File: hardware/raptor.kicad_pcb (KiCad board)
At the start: 4 copper layers, 22.9 x 57.7 mm, 70 parts, among them IC1 RAPTORQFN56, IC2 FT232H, IC3 MCP1755, IC4 93C56, IC5 TMUX1574RSVR, J1 USB, J11 CONN_20, J12 CONN_20, J2 Conn_01x02_Male, J3 Conn_01x02_Male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

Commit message: raptor hardware rev c
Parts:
- added U4: SN74LV1T34DCKR, parts and footprints:SOT65P210X110-5N, B.Cu at (141.5, 126.2)
- added U5: SN74LV1T34DCKR, parts and footprints:SOT65P210X110-5N, B.Cu at (145.9, 126.1)
- X1: footprint SamacSys_Parts:CSTNE12M0GH5L000R0 -> parts and footprints:CSTNE12M0GH5L000R0
- X2: value CSTNE12M0GH5L000R0 -> CSTCR6M25G55B-R0; footprint SamacSys_Parts:CSTNE12M0GH5L000R0 -> parts and footprints:CSTCR6M25G55BR0
- moved R24 3.77 mm to (147.7, 129.0), turned to 180 degrees
- moved X2 0.25 mm to (153.9, 112.9)
- moved U3 0.09 mm to (147.7, 130.9), turned to 180 degrees
- renumbered U1 to U3
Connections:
- IC2 pad 26: Net-(IC2-Pad26) -> Net-(D6-Pad1)
- IC2 pad 27: Net-(IC2-Pad27) -> Net-(D5-Pad1)
- IC2 pad 32: Net-(D6-Pad1) -> Net-(IC2-Pad32)
- IC2 pad 33: Net-(D5-Pad1) -> Net-(IC2-Pad33)
- IC5 pad 1: /RAPTOR_CS -> /USB_CS
- IC5 pad 16: /USB_CS -> /RAPTOR_CS
- IC5 pad 3: /USB_SI -> /RAPTOR_D1
- IC5 pad 4: /RAPTOR_D1 -> /USB_SI
- J12 pad 17: /PWM0 -> /PWM0_LV
- J12 pad 18: /PWM1 -> /PWM1_LV
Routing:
- net /TXD_EN: track 52.5 -> 69.5 mm
- net /USB_SO_RXD: track 53.4 -> 69.9 mm, vias 3 -> 4
- net GND: track 246.9 -> 260.5 mm, vias 12 -> 14
- net VDD: track 252.7 -> 265.7 mm
- net /PWM1_LV: track 0.00 -> 10.6 mm
- net /P0: track 62.0 -> 64.9 mm
- net /PWM0_LV: track 0.00 -> 2.82 mm
- net Net-(D5-Pad1): track 4.48 -> 7.25 mm
- net Net-(D6-Pad1): track 4.10 -> 6.53 mm
- net /TMUX_SEL: track 57.6 -> 59.1 mm
- net /RAPTOR_D1: track 51.0 -> 52.3 mm
- net /USB_SI: track 28.4 -> 27.1 mm
- net /USB_CS: track 18.1 -> 19.1 mm
- net /PWM0: track 19.0 -> 19.9 mm, vias 1 -> 2
- net /PWM1: track 18.6 -> 18.5 mm, vias 1 -> 2
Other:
- board text added: "CS1"
- board text added: "M_SEL"
- board text added: "OUT"
- board text added: "PW0"
- board text added: "PW1"
- board text added: "Rev C"
- board text added: "SCK1"
- board text added: "SDI1"
- board text added: "SDO1"
- board text added: "TX_EN"
- board text added: "VR+"
- board text added: "VR-"
- board text removed: "AOUT"
- board text removed: "MCS1"
- board text removed: "MSCK1"
- board text removed: "MSI1"
- board text removed: "MSO1"
- board text removed: "PWM0"
- board text removed: "PWM1"
- board text removed: "Rev B"
- board text removed: "TMUX_SEL"
- board text removed: "TXD_EN"
- board text removed: "VREF+"
- board text removed: "VREF-"

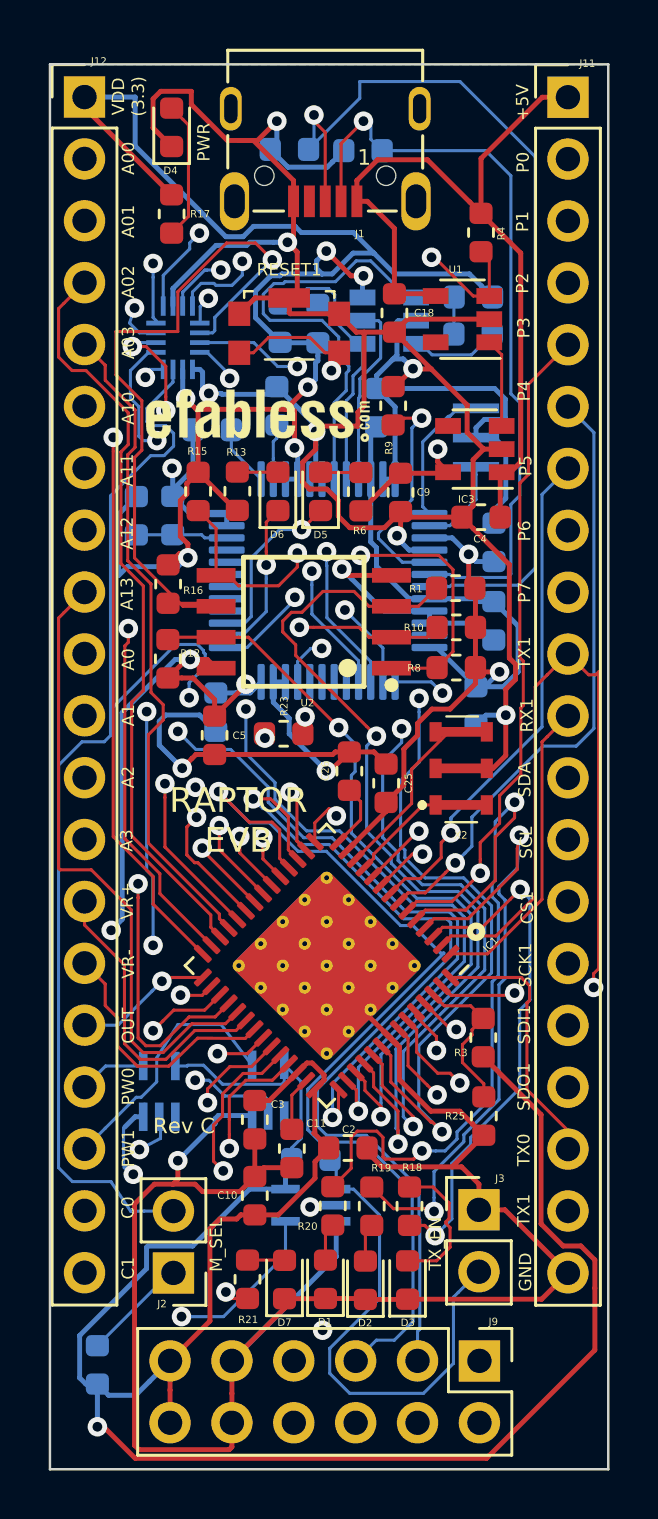
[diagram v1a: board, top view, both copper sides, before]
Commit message: updated raptor evb rev d
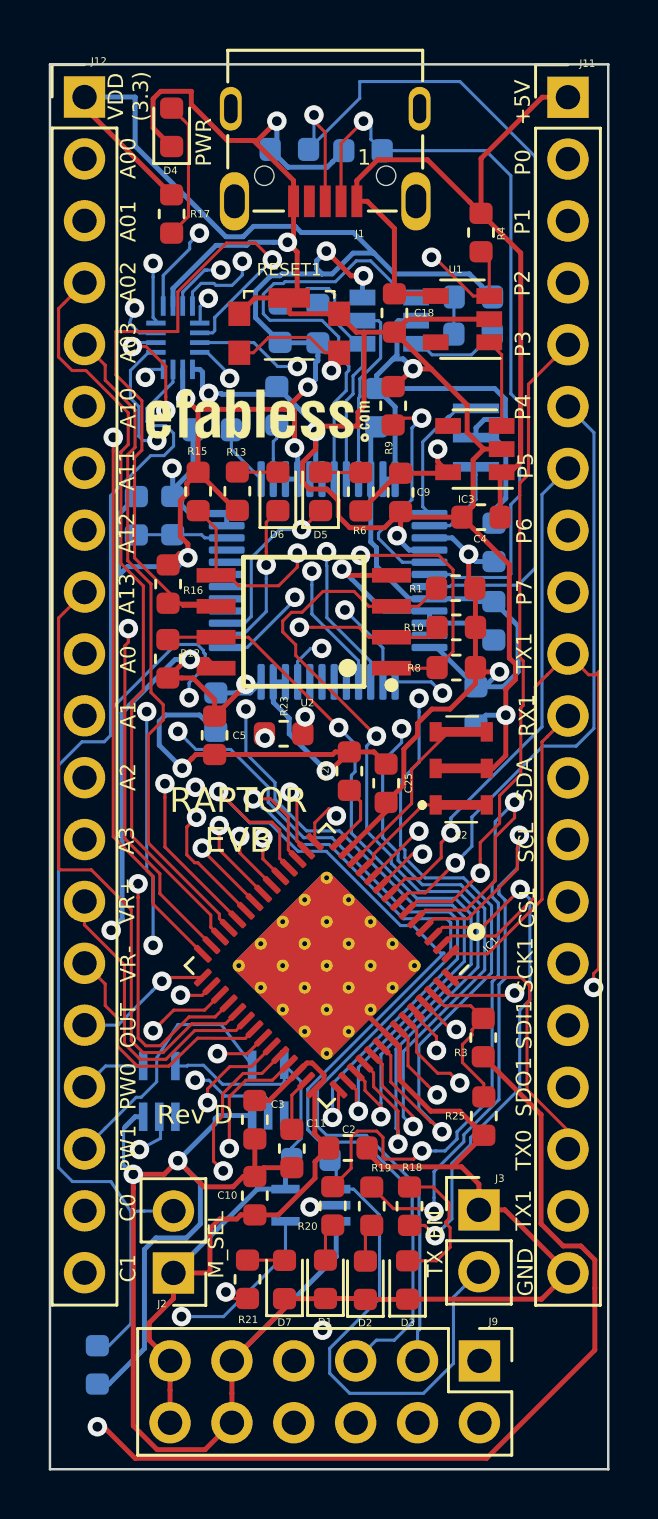
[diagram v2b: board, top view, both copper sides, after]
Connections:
- J2 pad 1: Net-(J2-Pad1) -> VDD
- R11 pad 1: Net-(J2-Pad1) -> /TMUX_SEL
- R11 pad 2: VDD -> GND
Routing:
- net GND: track 260.5 -> 269.9 mm
- net VDD: track 265.7 -> 256.9 mm
- net /TMUX_SEL: track 59.1 -> 65.5 mm
- net Net-(J2-Pad1): track 4.36 -> 0.00 mm
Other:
- board text added: "Rev D"
- board text removed: "Rev C"
